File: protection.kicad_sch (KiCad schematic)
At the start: 16 parts, among them Q1 Q_NMOS, Q5 Q_NMOS, Q9 Q_NMOS

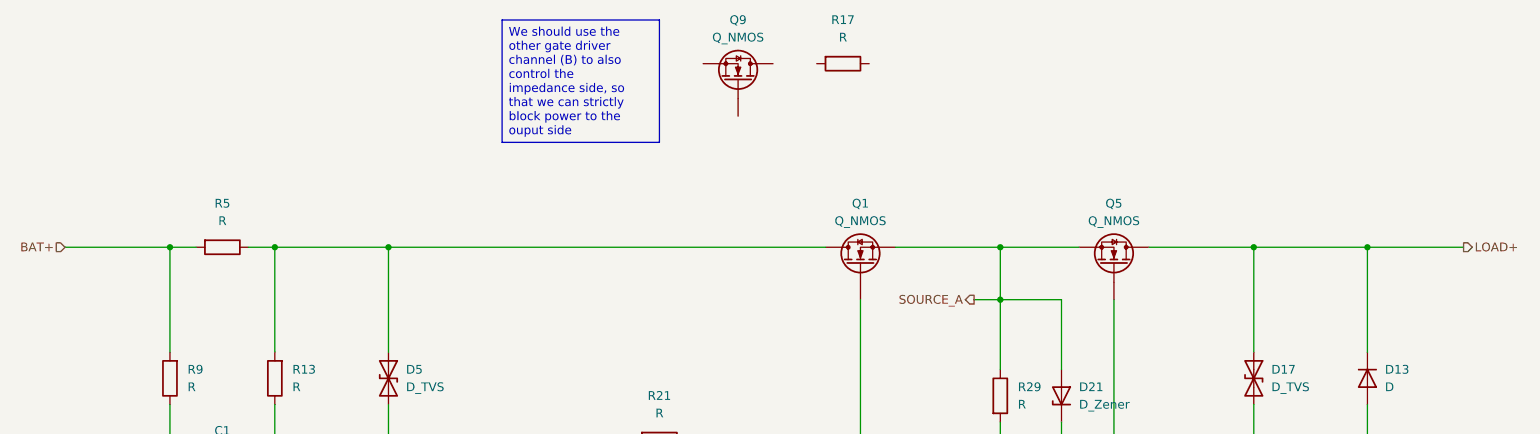
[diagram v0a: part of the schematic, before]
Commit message: Worked on the MCU page and the DC-DC page. Will still need to change a few things and add the buzzer and piezo stuff (#3)
Co-authored-by: Nima <nima.shirazi@flyzipline.com>
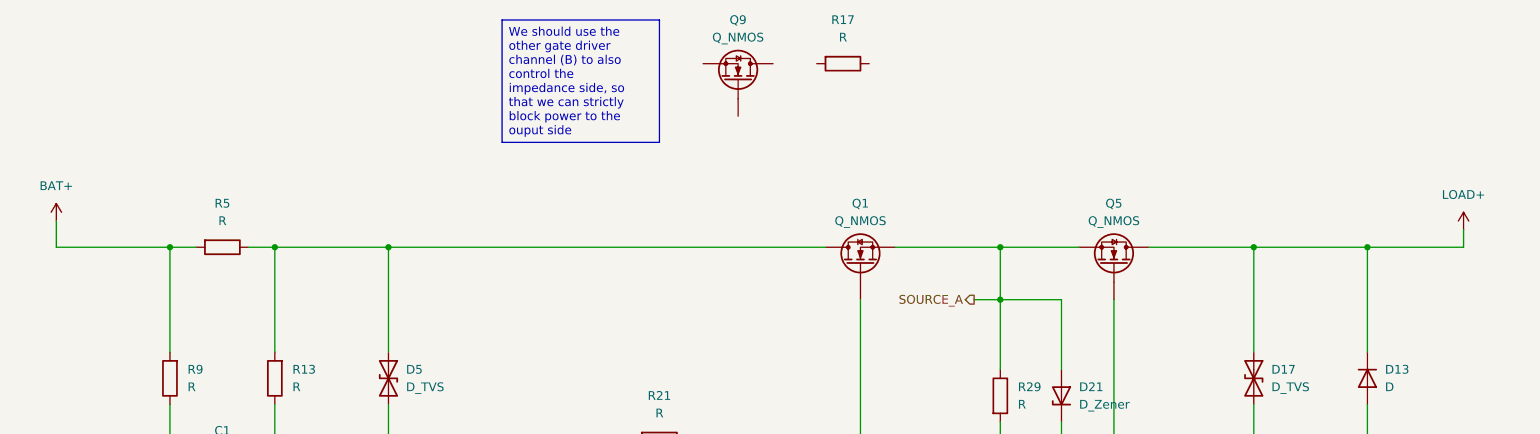
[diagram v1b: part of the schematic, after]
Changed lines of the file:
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@@
+	(wire
+		(pts
+			(xy 24.13 66.04) (xy 24.13 69.85)
+		)
+		(stroke
+			(width 0)
+			(type default)
+		)
+	)
 	(wire
 		(pts
@@
 	(wire
 		(pts
+			(xy 228.6 69.85) (xy 228.6 67.31)
+		)
+		(stroke
+			(width 0)
+			(type default)
+		)
+	)
+	(wire
+		(pts
 			(xy 127 104.14) (xy 127 97.79)
 		)
@@
 	(wire
 		(pts
-			(xy 25.4 69.85) (xy 40.64 69.85)
-		)
-		(stroke
-			(width 0)
-			(type default)
-		)
-	)
-	(wire
-		(pts
 			(xy 127 104.14) (xy 140.97 104.14)
 		)
@@
 		(pts
 			(xy 177.8 104.14) (xy 170.18 104.14)
+		)
+		(stroke
+			(width 0)
+			(type default)
+		)
+	)
+	(wire
+		(pts
+			(xy 24.13 69.85) (xy 40.64 69.85)
 		)
 		(stroke
@@
 		)
 	)
-	(hierarchical_label "BAT+"
-		(shape input)
-		(at 25.4 69.85 180)
-		(effects
-			(font
-				(size 1.27 1.27)
-			)
-			(justify right)
-		)
-	)
 	(hierarchical_label "IS_P"
 		(shape output)
@@
 		)
 	)
-	(hierarchical_label "LOAD+"
-		(shape output)
-		(at 228.6 69.85 0)
-		(effects
-			(font
-				(size 1.27 1.27)
-			)
-			(justify left)
-		)
-	)
 	(symbol
 		(lib_id "Device:R")
@@
 	)
 	(symbol
+		(lib_id "power:+3V3")
+		(at 228.6 67.31 0)
+		(unit 1)
+		(exclude_from_sim no)
+		(in_bom yes)
+		(on_board yes)
+		(dnp no)
+		(fields_autoplaced yes)
+		(property "Reference" "#PWR054"
+			(at 228.6 71.12 0)
+			(effects
+				(font
+					(size 1.27 1.27)
+				)
+				(hide yes)
+			)
+		)
+		(property "Value" "LOAD+"
+			(at 228.6 62.23 0)
+			(effects
+				(font
+					(size 1.27 1.27)
+				)
+			)
+		)
+		(property "Footprint" ""
+			(at 228.6 67.31 0)
+			(effects
+				(font
+					(size 1.27 1.27)
+				)
+				(hide yes)
+			)
+		)
+		(property "Datasheet" ""
+			(at 228.6 67.31 0)
+			(effects
+				(font
+					(size 1.27 1.27)
+				)
+				(hide yes)
+			)
+		)
+		(property "Description" "Power symbol creates a global label with name \"+3V3\""
+			(at 228.6 67.31 0)
+			(effects
+				(font
+					(size 1.27 1.27)
+				)
+				(hide yes)
+			)
+		)
+		(pin "1"
+		)
+		(instances
+			(project "battery_protector"
+				(path "/b2975477-3b95-446c-b662-4cca32764c73/60172fae-36a9-4c2c-a77c-3b2f4e907501"
+					(reference "#PWR054")
+					(unit 1)
+				)
+			)
+		)
+	)
+	(symbol
 		(lib_id "Device:Q_NMOS")
 		(at 123.19 45.72 270)
@@
 					(unit 1)
 				)
+			)
+		)
+	)
+	(symbol
+		(lib_id "power:+3V3")
+		(at 24.13 66.04 0)
+		(unit 1)
+		(exclude_from_sim no)
+		(in_bom yes)
+		(on_board yes)
+		(dnp no)
+		(fields_autoplaced yes)
+		(property "Reference" "#PWR053"
+			(at 24.13 69.85 0)
+			(effects
+				(font
+					(size 1.27 1.27)
+				)
+				(hide yes)
+			)
+		)
+		(property "Value" "BAT+"
+			(at 24.13 60.96 0)
+			(effects
+				(font
+					(size 1.27 1.27)
+				)
+			)
+		)
+		(property "Footprint" ""
+			(at 24.13 66.04 0)
+			(effects
+				(font
+					(size 1.27 1.27)
+				)
+				(hide yes)
+			)
+		)
+		(property "Datasheet" ""
+			(at 24.13 66.04 0)
+			(effects
+				(font
+					(size 1.27 1.27)
+				)
+				(hide yes)
+			)
+		)
+		(property "Description" "Power symbol creates a global label with name \"+3V3\""
+			(at 24.13 66.04 0)
+			(effects
+				(font
+					(size 1.27 1.27)
+				)
+				(hide yes)
+			)
+		)
+		(pin "1"
+		)
+		(instances
+			(project "battery_protector"
+				(path "/b2975477-3b95-446c-b662-4cca32764c73/60172fae-36a9-4c2c-a77c-3b2f4e907501"
+					(reference "#PWR053")
+					(unit 1)
+				)

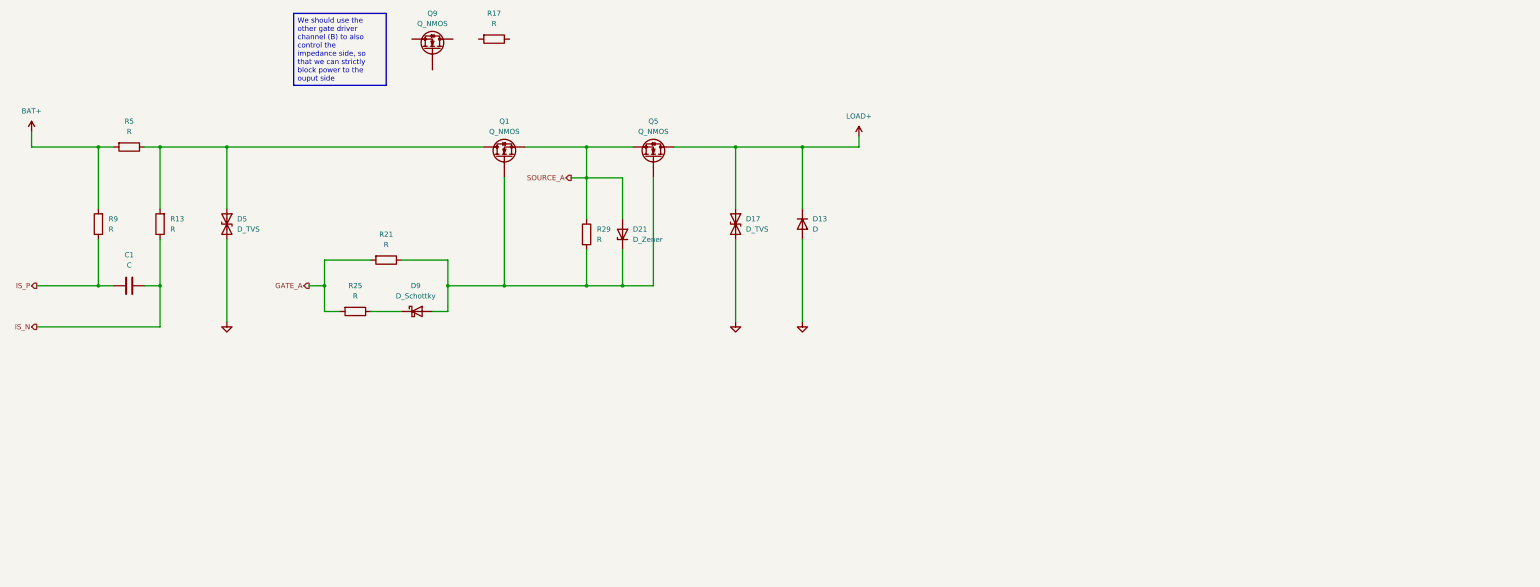
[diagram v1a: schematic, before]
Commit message: finish protection sheet
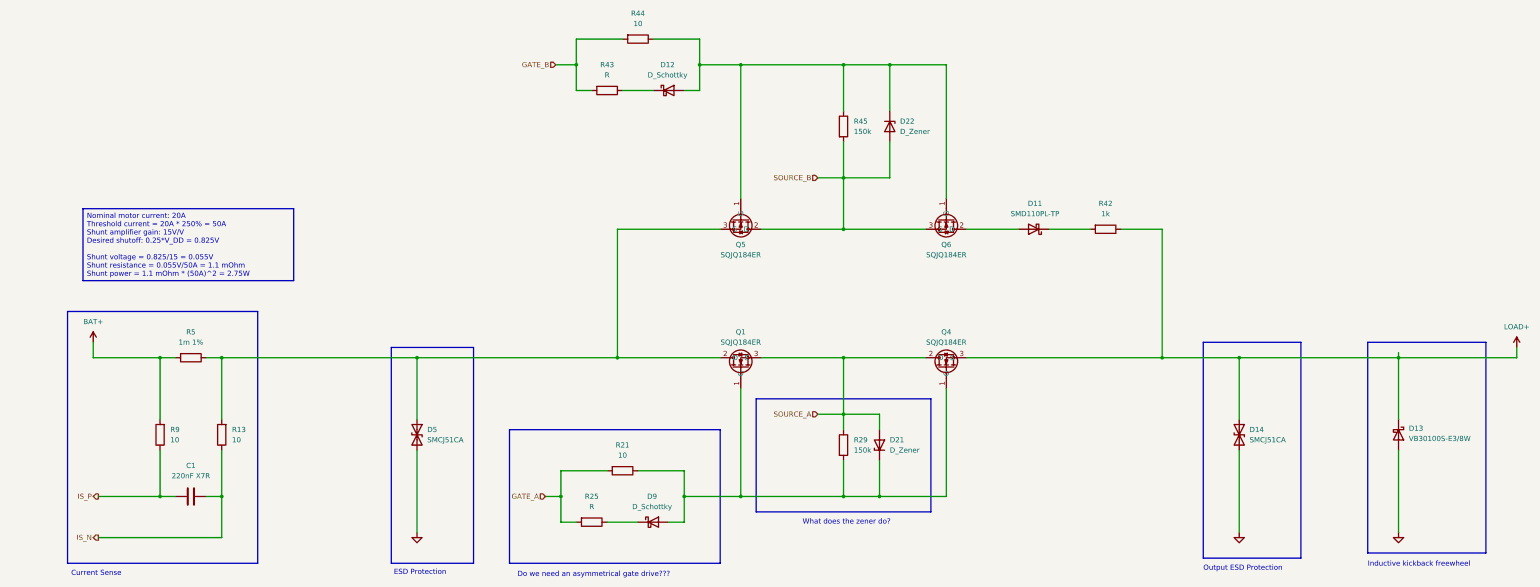
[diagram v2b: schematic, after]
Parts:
- removed D13: D, symbol Device:D
- removed D17: D_TVS, symbol Device:D_TVS
- removed Q1, Q5, Q9: Q_NMOS, symbol Device:Q_NMOS
- removed R17: R, symbol Device:R
- added D11: SMD110PL-TP, Diode_SMD:D_SOD-123F, symbol Device:D_Schottky
- added D12: D_Schottky, symbol Device:D_Schottky
- added D13: VB30100S-E3/8W, custom_footprints:VB30100S-E38W, symbol Device:D_Schottky
- added D14: SMCJ51CA, Diode_SMD:D_SMC, symbol Device:D_TVS
- added D22: D_Zener, symbol Device:D_Zener
- added Q1, Q4, Q5, Q6: SQJQ184ER, custom_footprints:SQJQ184ER, symbol custom_symbols:SQJQ184ER
- added R42: 1k, Resistor_SMD:R_0603_1608Metric, symbol Device:R
- added R43: R, symbol Device:R
- added R44: 10, Resistor_SMD:R_0603_1608Metric, symbol Device:R
- added R45: 150k, Resistor_SMD:R_0603_1608Metric, symbol Device:R
- C1: value C -> 220nF X7R; footprint (none) -> Capacitor_SMD:C_0603_1608Metric
- D5: value D_TVS -> SMCJ51CA; footprint (none) -> Diode_SMD:D_SMC
- R13, R21, R9: value R -> 10; footprint (none) -> Resistor_SMD:R_0603_1608Metric
- R29: value R -> 150k; footprint (none) -> Resistor_SMD:R_0603_1608Metric
- R5: value R -> 1m 1%; footprint (none) -> Resistor_SMD:R_2512_6332Metric; PN (none) -> SCMM2512S5-R001F
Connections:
- net GND: now also D13.2 (A), D14.2 (A2)
- net LOAD+: now also D13.1 (K), D14.1 (A1), Q4.3 (S), R42.1
- net SOURCE_A: now also Q1.3 (S), Q4.2 (D)
- net at D5.1 (A1), R13.2, R5.1: now also Q1.2 (D), Q5.3 (S)
- net at D21.1 (K), D9.2 (A), R21.1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: now also Q1.1 (G), Q4.1 (G)
- new net: D12.1 (K), R43.1
- new net: D12.2 (A), D22.1 (K), Q5.1 (G), Q6.1 (G), R44.1, R45.1
- new net: D11.1 (K), R42.2
- new net: D11.2 (A), Q6.2 (D)
- new net GATE_B: R43.2, R44.2
- new net SOURCE_B: D22.2 (A), Q5.2 (D), Q6.3 (S), R45.2
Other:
- note added: "Current Sense"
- note added: "Do we need an asymmetrical gate drive???"
- note added: "ESD Protection"
- note added: "Inductive kickback freewheel"
- note added: "Output ESD Protection"
- note added: "What does the zener do?"
- moved on the sheet: C1, D21, D5, D9, R13, R21, R25, R29, R5, R9

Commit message: jul 2 design review
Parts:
- removed D11: SMD110PL-TP, Diode_SMD:D_SOD-123F, symbol Device:D_Schottky
- removed D12, D9: D_Schottky, symbol Device:D_Schottky
- removed D21, D22: D_Zener, symbol Device:D_Zener
- added D26, D27: STPS3L60U, custom_footprints:STPS3L60U, symbol Device:D_Schottky
- C1: value 220nF X7R -> 150nF X7R; PN (none) -> CC0603JRX7R9BB154
- R21, R44: value 10 -> 100
- R25, R43: value R -> 10; footprint (none) -> Resistor_SMD:R_0603_1608Metric
- R5: value 1m 1% -> 1m 1% 3W; footprint Resistor_SMD:R_2512_6332Metric -> custom_footprints:WSK12161L000FEA; PN SCMM2512S5-R001F -> WSK12161L000FEA
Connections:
- net LOAD+: now also Q4.2 (D); no longer Q4.3 (S)
- net SOURCE_A: now also Q4.3 (S); no longer Q4.2 (D)
- net SOURCE_B: now also Q6.2 (D); no longer Q6.3 (S)
- net at Q1.1 (G), Q4.1 (G), R21.1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: now also D26.2 (A)
- net at R43.1: now also D27.1 (K)
- net at Q5.1 (G), Q6.1 (G), R44.1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: now also D27.2 (A)
- net at R42.2: now also Q6.3 (S)
- net at R25.1: now also D26.1 (K)
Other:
- note added: "Asymmetrical gate drive: slower turn-on"
- note removed: "Do we need an asymmetrical gate drive???"
- note removed: "What does the zener do?"
- moved on the sheet: R42

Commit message: Added footprints to resistors and capacitors, and fixed the mosfets wiring issue (#4)
Jul9th push. Added footprints to resistors and capacitors, and fixed the mosfets wiring issue
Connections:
- net SOURCE_B: now also Q5.3 (S), Q6.3 (S); no longer Q5.2 (D), Q6.2 (D)
- net at D5.1 (A1), Q1.2 (D), R13.2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: now also Q5.2 (D); no longer Q5.3 (S)
- net at R42.2: now also Q6.2 (D); no longer Q6.3 (S)
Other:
- moved on the sheet: Q5, Q6
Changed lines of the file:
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@@
+		)
+	)
+	(text_box "Due to the intrinsic inductance of the shunt leads, we need an RC snubber circuit to zero the reactance (resonance)\n\nR_shunt/L = 1/RC -> C=150nF"
+		(exclude_from_sim no)
+		(at 33.02 180.34 0)
+		(size 46.99 13.97)
+		(margins 0.9525 0.9525 0.9525 0.9525)
+		(stroke
+			(width 0)
+			(type solid)
+		)
+		(fill
+			(type none)
+		)
+		(effects
+			(font
+				(size 1.27 1.27)
+			)
+			(justify left top)
 		)
 	)
@@
 			)
 		)
-		(property "Datasheet" "https://www.mccsemi.com/pdf/Products/SMD110PL-SMD1200PL(SOD-123FL).pdf"
+		(property "Datasheet" "https://www.vishay.com/docs/88941/v30100s.pdf"
 			(at 361.95 140.97 0)
 			(effects
@@
 	(symbol
 		(lib_id "custom_symbols:SQJQ184ER")
-		(at 201.93 81.28 270)
+		(at 196.85 81.28 90)
+		(mirror x)
 		(unit 1)
 		(exclude_from_sim no)
@@
 		(on_board yes)
 		(dnp no)
-		(fields_autoplaced yes)
 		(property "Reference" "Q5"
 			(at 199.39 93.98 90)
@@
 		)
 		(property "Footprint" "custom_footprints:SQJQ184ER"
-			(at 201.93 81.28 0)
+			(at 196.85 81.28 0)
 			(effects
 				(font
@@
 		)
 		(property "Datasheet" "https://www.vishay.com/docs/71298/sqjq184er.pdf"
-			(at 201.93 81.28 0)
+			(at 196.85 81.28 0)
 			(effects
 				(font
@@
 		)
 		(property "Description" "Automotive N-Channel 80 V (D-S) 175 °C MOSFET"
-			(at 201.93 81.28 0)
+			(at 196.85 81.28 0)
 			(effects
 				(font
@@
 	(symbol
 		(lib_id "custom_symbols:SQJQ184ER")
-		(at 247.65 81.28 90)
-		(mirror x)
+		(at 252.73 81.28 270)
 		(unit 1)
 		(exclude_from_sim no)
@@
 		)
 		(property "Footprint" "custom_footprints:SQJQ184ER"
-			(at 247.65 81.28 0)
+			(at 252.73 81.28 0)
 			(effects
 				(font
@@
 		)
 		(property "Datasheet" "https://www.vishay.com/docs/71298/sqjq184er.pdf"
-			(at 247.65 81.28 0)
+			(at 252.73 81.28 0)
 			(effects
 				(font
@@
 		)
 		(property "Description" "Automotive N-Channel 80 V (D-S) 175 °C MOSFET"
-			(at 247.65 81.28 0)
-			(effects
-				(font
+			(at 252.73 81.28 0)
+			(effects
+				(font

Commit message: finish schematic
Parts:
- renumbered D26 to D6, D27 to D7, D14 to D8, D13 to D9, Q5 to Q1, Q1 to Q2, Q6 to Q3, R21 to R10, R44 to R11, R45 to R12, R29 to R13, R42 to R14, R9 to R5, R5 to R6, R13 to R7, R25 to R8, R43 to R9

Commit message: setup layout rules
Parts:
- removed D9: VB30100S-E3/8W, custom_footprints:VB30100S-E38W, symbol Device:D_Schottky
- added D15: D_Schottky_AAK, custom_footprints:VB30100S-E38W, symbol Device:D_Schottky_AAK
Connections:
- net GND: now also D15.1 (A)
- net LOAD+: now also D15.3 (K)
- no-connect marks 0 -> 1
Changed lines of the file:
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@@
 		(color 0 0 0 0)
 	)
+	(no_connect
+		(at 361.95 146.05)
+	)
 	(wire
 		(pts
@@
 	(wire
 		(pts
+			(xy 364.49 146.05) (xy 364.49 165.1)
+		)
+		(stroke
+			(width 0)
+			(type default)
+		)
+	)
+	(wire
+		(pts
 			(xy 322.58 121.92) (xy 322.58 137.16)
 		)
@@
 		(pts
 			(xy 199.39 129.54) (xy 199.39 156.21)
-		)
-		(stroke
-			(width 0)
-			(type default)
-		)
-	)
-	(wire
-		(pts
-			(xy 361.95 144.78) (xy 361.95 165.1)
 		)
 		(stroke
@@
 	(symbol
 		(lib_id "power:GND")
-		(at 361.95 165.1 0)
+		(at 364.49 165.1 0)
 		(unit 1)
 		(exclude_from_sim no)
@@
 		(fields_autoplaced yes)
 		(property "Reference" "#PWR0120"
-			(at 361.95 171.45 0)
+			(at 364.49 171.45 0)
 			(effects
 				(font
@@
 		)
 		(property "Value" "GND"
-			(at 361.95 170.18 0)
+			(at 364.49 170.18 0)
 			(effects
 				(font
@@
 		)
 		(property "Footprint" ""
-			(at 361.95 165.1 0)
+			(at 364.49 165.1 0)
 			(effects
 				(font
@@
 		)
 		(property "Datasheet" ""
-			(at 361.95 165.1 0)
+			(at 364.49 165.1 0)
 			(effects
 				(font
@@
 		)
 		(property "Description" "Power symbol creates a global label with name \"GND\" , ground"
-			(at 361.95 165.1 0)
+			(at 364.49 165.1 0)
 			(effects
 				(font
@@
 	)
 	(symbol
-		(lib_id "Device:D_Schottky")
-		(at 361.95 140.97 270)
-		(unit 1)
-		(exclude_from_sim no)
-		(in_bom yes)
-		(on_board yes)
-		(dnp no)
-		(fields_autoplaced yes)
-		(property "Reference" "D9"
-			(at 364.49 139.3824 90)
-			(effects
-				(font
-					(size 1.27 1.27)
-				)
-				(justify left)
-			)
-		)
-		(property "Value" "VB30100S-E3/8W"
-			(at 364.49 141.9224 90)
-			(effects
-				(font
-					(size 1.27 1.27)
-				)
-				(justify left)
-			)
-		)
-		(property "Footprint" "custom_footprints:VB30100S-E38W"
-			(at 361.95 140.97 0)
-			(effects
-				(font
-					(size 1.27 1.27)
-				)
-				(hide yes)
-			)
-		)
-		(property "Datasheet" "https://www.vishay.com/docs/88941/v30100s.pdf"
-			(at 361.95 140.97 0)
-			(effects
-				(font
-					(size 1.27 1.27)
-				)
-				(hide yes)
-			)
-		)
-		(property "Description" "Schottky diode"
-			(at 361.95 140.97 0)
-			(effects
-				(font
-					(size 1.27 1.27)
-				)
-				(hide yes)
-			)
-		)
-		(pin "1"
-		)
-		(pin "2"
-		)
-		(instances
-			(project "battery_protector"
-				(path "/b2975477-3b95-446c-b662-4cca32764c73/60172fae-36a9-4c2c-a77c-3b2f4e907501"
-					(reference "D9")
-					(unit 1)
-				)
-			)
-		)
-	)
-	(symbol
 		(lib_id "Device:D_TVS")
 		(at 322.58 140.97 270)
@@
 					(unit 1)
 				)
+			)
+		)
+	)
+	(symbol
+		(lib_id "Device:D_Schottky_AAK")
+		(at 361.95 140.97 270)
+		(unit 1)
+		(exclude_from_sim no)
+		(in_bom yes)
+		(on_board yes)
+		(dnp no)
+		(fields_autoplaced yes)
+		(property "Reference" "D15"
+			(at 365.76 140.5889 90)
+			(effects
+				(font
+					(size 1.27 1.27)
+				)
+				(justify left)
+			)
+		)
+		(property "Value" "D_Schottky_AAK"
+			(at 365.76 143.1289 90)
+			(effects
+				(font
+					(size 1.27 1.27)
+				)
+				(justify left)
+			)
+		)
+		(property "Footprint" "custom_footprints:VB30100S-E38W"
+			(at 361.95 140.97 0)
+			(effects
+				(font
+					(size 1.27 1.27)
+				)
+				(hide yes)
+			)
+		)
+		(property "Datasheet" "https://www.vishay.com/docs/88941/v30100s.pdf"
+			(at 361.95 140.97 0)
+			(effects
+				(font
+					(size 1.27 1.27)
+				)
+				(hide yes)
+			)
+		)
+		(property "Description" "Schottky diode, anode on pins 1 and 2"
+			(at 361.95 140.97 0)
+			(effects
+				(font
+					(size 1.27 1.27)
+				)
+				(hide yes)
+			)
+		)
+		(pin "1"
+		)
+		(pin "2"
+		)
+		(pin "3"
+		)
+		(instances
+			(project ""
+				(path "/b2975477-3b95-446c-b662-4cca32764c73/60172fae-36a9-4c2c-a77c-3b2f4e907501"
+					(reference "D15")
+					(unit 1)
+				)
